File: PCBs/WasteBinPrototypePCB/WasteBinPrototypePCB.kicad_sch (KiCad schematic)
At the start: 0 parts

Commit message: added peltier design to schematic
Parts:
- added D?: D, symbol Device:D
- added D?: DIODE-1N4148, Diode_SMD:D_1206_3216Metric_Pad1.42x1.75mm_HandSolder, symbol SparkFun-DiscreteSemi:DIODE-1N4148
- added D?: LED, symbol Device:LED
- added PE?: PeltierElement, SamacSys_Parts:1808190, symbol Device:PeltierElement
- added Q?: IRL540NSTRLPBF, IRF2804STRLPBF, symbol SamacSys_Parts:IRL540NSTRLPBF
- added R? (x3): 4.7K, symbol Device:R
- added R?: 100, symbol Device:R
- added R?: 1K, symbol Device:R
- added U?: PC817, Package_DIP:DIP-4_W7.62mm, symbol Isolator:PC817
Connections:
- new net: Q?.1, R?.1, R?.1
- new net: D?.2 (A), PE?.2, Q?.3, R?.2
- new net: D?.1 (K), R?.2, U?.3
- new net: R?.1, U?.1
- new net: R?.2, U?.4
- new net: D?.1 (K), R?.1
- new net 12V+: D?.1 (C), D?.2 (A), PE?.1, R?.1
- new net GND: D?.2 (A), Q?.2, R?.2, U?.2
- new net PWM: R?.2
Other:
- note added: "Peltier Element"

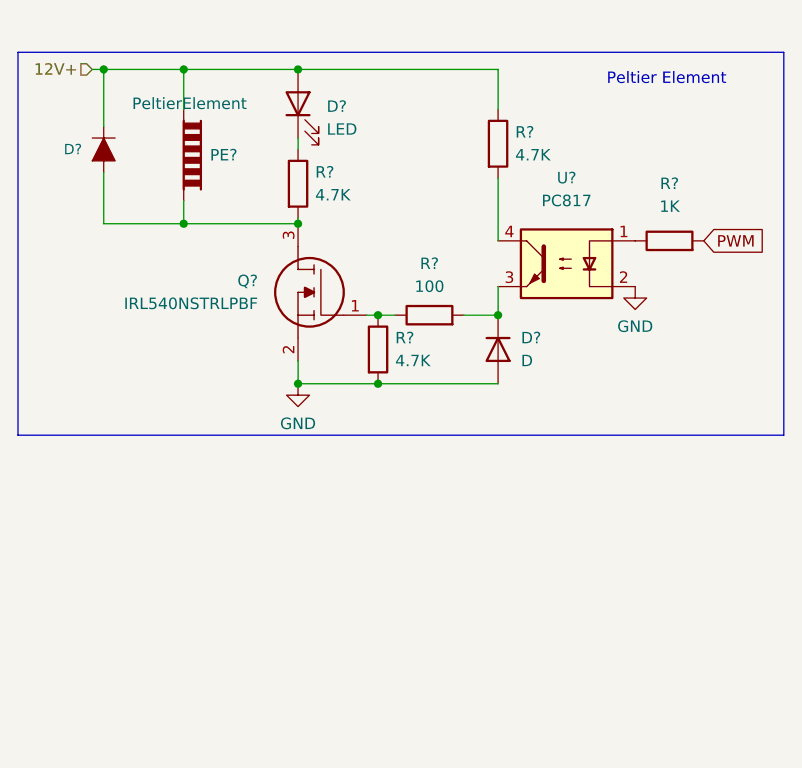
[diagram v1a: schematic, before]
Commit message: added piezo speaker to schematic
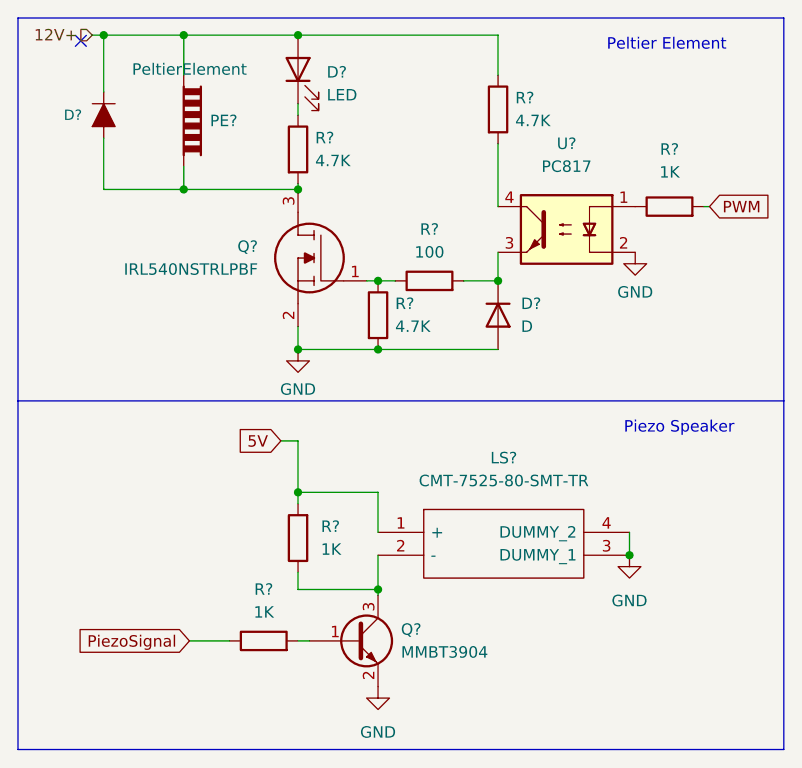
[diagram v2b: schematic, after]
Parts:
- added LS?: CMT-7525-80-SMT-TR, CMT752580SMTTR, symbol SamacSys_Parts:CMT-7525-80-SMT-TR
- added Q?: MMBT3904, Package_TO_SOT_SMD:SOT-23, symbol Transistor_BJT:MMBT3904
- added R? (x2): 1K, symbol Device:R
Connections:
- net GND: now also LS?.3 (DUMMY_1), LS?.4 (DUMMY_2), Q?.2 (E)
- new net: Q?.1 (B), R?.2
- new net: LS?.2 (-), Q?.3 (C), R?.1
- new net 5V: LS?.1 (+), R?.2
- new net PiezoSignal: R?.1
- no-connect marks 0 -> 1
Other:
- note added: "Piezo Speaker"
- moved on the sheet: D?, PE?, Q?, R?, U?

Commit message: added Hall effect sensor to schematic
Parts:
- added R?: 10K, symbol Device:R
- added U?: A1301EUA-T, symbol Sensor_Magnetic:A1301EUA-T
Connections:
- net 5V: now also R?.2, U?.1 (VCC)
- net GND: now also U?.2 (GND)
- new net HES: R?.1, U?.3 (VOUT)
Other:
- note added: "Hall Effect Sensor"
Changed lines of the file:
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@@
   (junction (at 43.815 14.605) (diameter 0) (color 0 0 0 0)
+  )
+  (junction (at 52.07 115.57) (diameter 0) (color 0 0 0 0)
   )
   (junction (at 43.815 49.53) (diameter 0) (color 0 0 0 0)
@@
     (stroke (width 0) (type default) (color 0 0 0 0))
   )
+  (wire (pts (xy 52.07 118.745) (xy 53.975 118.745))
+    (stroke (width 0) (type default) (color 0 0 0 0))
+  )
   (wire (pts (xy 43.815 31.115) (xy 43.815 31.75))
     (stroke (width 0) (type default) (color 0 0 0 0))
   )
+  (wire (pts (xy 52.07 114.935) (xy 52.07 115.57))
+    (stroke (width 0) (type default) (color 0 0 0 0))
+  )
   (wire (pts (xy 43.815 23.495) (xy 43.815 22.225))
     (stroke (width 0) (type default) (color 0 0 0 0))
@@
     (stroke (width 0) (type default) (color 0 0 0 0))
   )
+  (polyline (pts (xy 97.79 93.98) (xy 97.79 123.825))
+    (stroke (width 0) (type default) (color 0 0 0 0))
+  )
+  (wire (pts (xy 52.07 115.57) (xy 52.07 118.745))
+    (stroke (width 0) (type default) (color 0 0 0 0))
+  )
   (wire (pts (xy 31.75 81.915) (xy 36.195 81.915))
     (stroke (width 0) (type default) (color 0 0 0 0))
@@
     (stroke (width 0) (type default) (color 0 0 0 0))
   )
+  (wire (pts (xy 52.07 115.57) (xy 62.23 115.57))
+    (stroke (width 0) (type default) (color 0 0 0 0))
+  )
   (wire (pts (xy 43.815 65.405) (xy 43.815 59.69))
     (stroke (width 0) (type default) (color 0 0 0 0))
@@
     (stroke (width 0) (type default) (color 0 0 0 0))
   )
+  (polyline (pts (xy 97.79 123.825) (xy 12.7 123.825))
+    (stroke (width 0) (type default) (color 0 0 0 0))
+  )
   (wire (pts (xy 52.705 76.835) (xy 52.705 76.2))
     (stroke (width 0) (type default) (color 0 0 0 0))
@@
     (stroke (width 0) (type default) (color 0 0 0 0))
   )
+  (polyline (pts (xy 12.7 123.825) (xy 12.7 93.98))
+    (stroke (width 0) (type default) (color 0 0 0 0))
+  )
   (wire (pts (xy 52.705 65.405) (xy 43.815 65.405))
     (stroke (width 0) (type default) (color 0 0 0 0))
@@
     (stroke (width 0) (type default) (color 0 0 0 0))
   )
+  (wire (pts (xy 62.23 107.95) (xy 62.23 104.775))
+    (stroke (width 0) (type default) (color 0 0 0 0))
+  )
   (polyline (pts (xy 97.79 55.245) (xy 97.79 12.7))
     (stroke (width 0) (type default) (color 0 0 0 0))
@@
   (wire (pts (xy 43.815 14.605) (xy 66.04 14.605))
     (stroke (width 0) (type default) (color 0 0 0 0))
+  )
+  (text "Hall Effect Sensor" (at 77.47 97.155 0)
+    (effects (font (size 1.27 1.27)) (justify left bottom))
   )
   (text "Peltier Element" (at 78.105 16.51 0)
@@
     )
   )
+  (global_label "5V" (shape input) (at 62.23 104.775 0) (fields_autoplaced)
+    (effects (font (size 1.27 1.27)) (justify left))
+    (property "Intersheet References" "${INTERSHEET_REFS}" (id 0) (at 66.9412 104.6956 0)
+      (effects (font (size 1.27 1.27)) (justify left) hide)
+    )
+  )
+  (global_label "HES" (shape input) (at 53.975 118.745 0) (fields_autoplaced)
+    (effects (font (size 1.27 1.27)) (justify left))
+    (property "Intersheet References" "${INTERSHEET_REFS}" (id 0) (at 60.0771 118.6656 0)
+      (effects (font (size 1.27 1.27)) (justify left) hide)
+    )
+  )
   (hierarchical_label "12V+" (shape input) (at 20.955 14.605 180)
     (effects (font (size 1.27 1.27)) (justify right))
@@
     )
     (property "Datasheet" "~" (id 3) (at 52.705 45.72 0)
+      (effects (font (size 1.27 1.27)) hide)
+    )
+    (pin "1")
+    (pin "2")
+  )
+  (symbol (lib_id "Device:R") (at 62.23 111.76 180) (unit 1)
+    (in_bom yes) (on_board yes) (fields_autoplaced)
+    (property "Reference" "R?" (id 0) (at 64.135 110.4899 0)
+      (effects (font (size 1.27 1.27)) (justify right))
+    )
+    (property "Value" "10K" (id 1) (at 64.135 113.0299 0)
+      (effects (font (size 1.27 1.27)) (justify right))
+    )
+    (property "Footprint" "" (id 2) (at 64.008 111.76 90)
+      (effects (font (size 1.27 1.27)) hide)
+    )
+    (property "Datasheet" "~" (id 3) (at 62.23 111.76 0)
       (effects (font (size 1.27 1.27)) hide)
     )
@@
     (pin "1")
     (pin "2")
+  )
+  (symbol (lib_id "power:GND") (at 41.91 104.775 0) (unit 1)
+    (in_bom yes) (on_board yes) (fields_autoplaced)
+    (property "Reference" "#PWR?" (id 0) (at 41.91 111.125 0)
+      (effects (font (size 1.27 1.27)) hide)
+    )
+    (property "Value" "GND" (id 1) (at 41.91 109.855 0))
+    (property "Footprint" "" (id 2) (at 41.91 104.775 0)
+      (effects (font (size 1.27 1.27)) hide)
+    )
+    (property "Datasheet" "" (id 3) (at 41.91 104.775 0)
+      (effects (font (size 1.27 1.27)) hide)
+    )
+    (pin "1")
   )
   (symbol (lib_id "power:GND") (at 80.645 72.39 0) (unit 1)
@@
     (pin "1")
   )
+  (symbol (lib_id "Sensor_Magnetic:A1301EUA-T") (at 52.07 107.315 270) (unit 1)
+    (in_bom yes) (on_board yes) (fields_autoplaced)
+    (property "Reference" "U?" (id 0) (at 52.07 96.52 90))
+    (property "Value" "A1301EUA-T" (id 1) (at 52.07 99.06 90))
+    (property "Footprint" "" (id 2) (at 43.18 107.315 0)
+      (effects (font (size 1.27 1.27) italic) (justify left) hide)
+    )
+    (property "Datasheet" "http://www.allegromicro.com/~/media/Files/Datasheets/A1301-2-Datasheet.ashx" (id 3) (at 52.07 104.775 0)
+      (effects (font (size 1.27 1.27)) hide)
+    )
+    (pin "1")
+    (pin "2")
+    (pin "3")
+  )
   (symbol (lib_id "Device:LED") (at 43.815 18.415 90) (unit 1)
     (in_bom yes) (on_board yes) (fields_autoplaced)
@@
       (reference "#PWR?") (unit 1) (value "GND") (footprint "")
     )
+    (path "/5a17defd-9142-4224-865d-f4648153ba82"
+      (reference "#PWR?") (unit 1) (value "GND") (footprint "")
+    )
     (path "/666e1366-8b99-45ca-af58-37cd07d0f351"
       (reference "#PWR?") (unit 1) (value "GND") (footprint "")
@@
       (reference "R?") (unit 1) (value "4.7K") (footprint "")
     )
+    (path "/23a0a120-4468-43ee-9d86-86770507e5ab"
+      (reference "R?") (unit 1) (value "10K") (footprint "")
+    )
     (path "/4583b515-ed49-4672-843a-9aa019653137"
       (reference "R?") (unit 1) (value "100") (footprint "")
@@
       (reference "U?") (unit 1) (value "PC817") (footprint "Package_DIP:DIP-4_W7.62mm")
     )
-  )
+    (path "/d6911078-c811-4b16-81c1-2d59c3e06949"
+      (reference "U?") (unit 1) (value "A1301EUA-T") (footprint "")
+    )
+  )

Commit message: improved on documentation and design
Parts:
- added C? (x2): 2.2uF 25V, symbol Device:C
- added IC?: MCP1793T-3302H_OT, SOT95P280X145-5N, symbol SamacSys_Parts:MCP1793T-3302H_OT
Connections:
- net 12V+: now also C?.2, IC?.1 (VIN), IC?.3 (~{SHDN})
- net GND: now also C?.1, C?.2, IC?.2 (GND)
- net 5V renamed 3.3V
- net 3.3V: now also C?.1, IC?.5 (VOUT)
- no-connect marks 1 -> 0
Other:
- note added: "Vragen voor insyte: -ESP32 devkit direct op pcb (d.m.v. headers)? -> scheelt ontwerptijd en geeft flexibiliteit -Handsolderen of pcb asemblage door bedrijf? -temperatuur sensor plaatsing en type (SHT40 of goedkoper alternatief?) -klep sensor (HES), plaatsing en beeld hierover. -2 printplaten 1 als devkit en 1 voor eindresultaat."

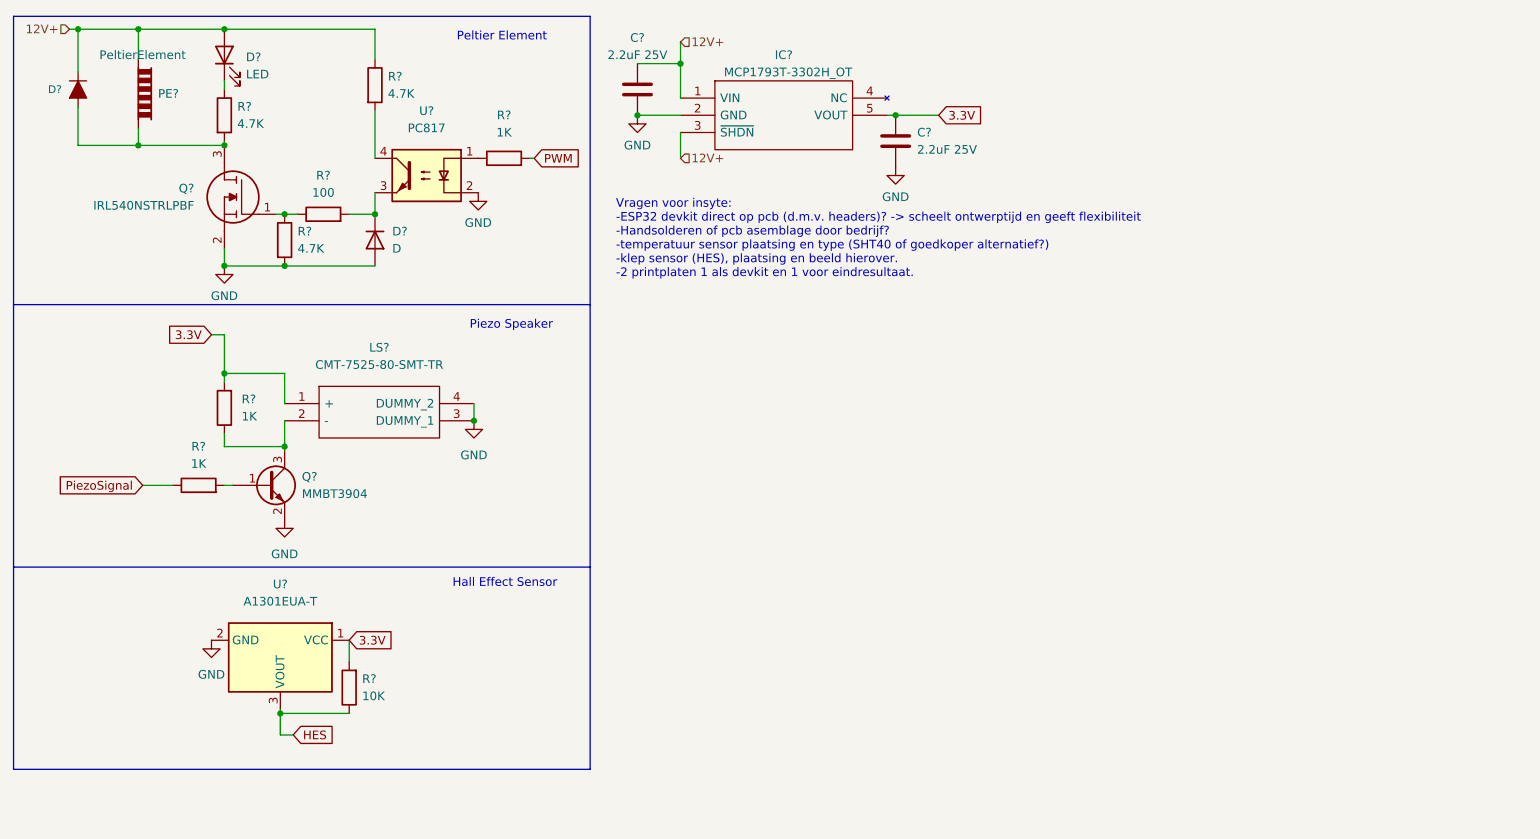
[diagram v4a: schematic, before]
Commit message: added microcontroller, breakout headers, 5V regulator and i2c vreakout to schematic
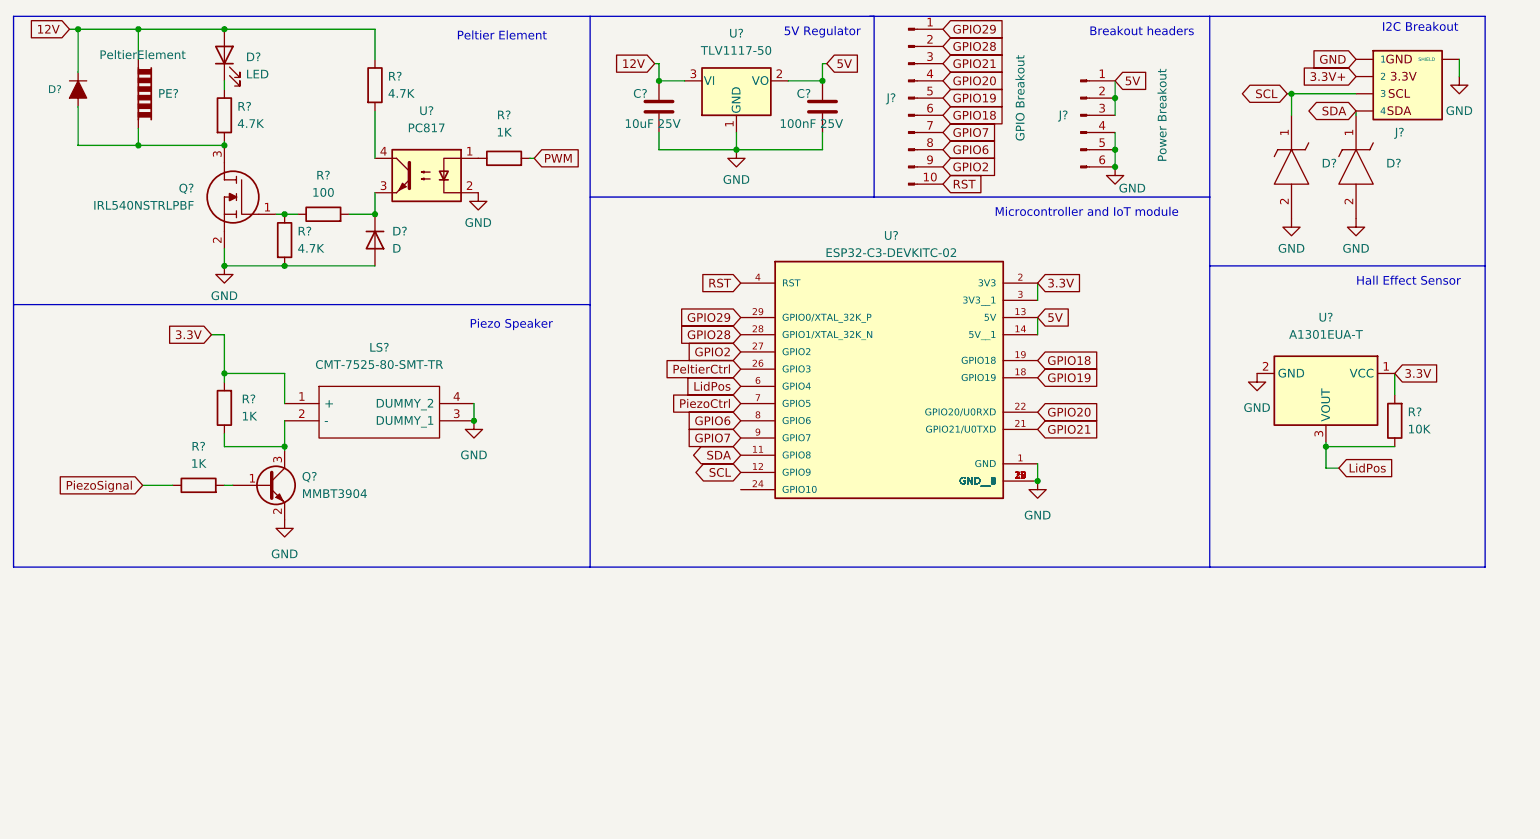
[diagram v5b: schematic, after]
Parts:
- removed C? (x2): 2.2uF 25V, symbol Device:C
- removed IC?: MCP1793T-3302H_OT, SOT95P280X145-5N, symbol SamacSys_Parts:MCP1793T-3302H_OT
- added C?: 100nF 25V, Capacitor_SMD:C_0805_2012Metric_Pad1.18x1.45mm_HandSolder, symbol Device:C
- added C?: 10uF 25V, Capacitor_SMD:C_0805_2012Metric_Pad1.18x1.45mm_HandSolder, symbol Device:C
- added D? (x2): ESD7351HT1G, SamacSys_Parts:SOD2512X110N, symbol SamacSys_Parts:ESD7351HT1G
- added J?: Conn_01x06_Male, symbol Connector:Conn_01x06_Male
- added J?: SM04B-SRSS-TB(LF)(SN), SnapEDA Library:JST_SM04B-SRSS-TB(LF)(SN), symbol SM04B-SRSS-TB_LF__SN_:SM04B-SRSS-TB(LF)(SN)
- added J?: Conn_01x10_Male, symbol Connector:Conn_01x10_Male
- added U?: TLV1117-50, symbol Regulator_Linear:TLV1117-50
- added U?: ESP32-C3-DEVKITC-02, SnapEDA Library:XCVR_ESP32-C3-DEVKITC-02, symbol ESP32-C3-DEVKITC-02:ESP32-C3-DEVKITC-02
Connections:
- net 3.3V: now also U?.2 (3V3), U?.3 (3V3__1)
- net GND: now also C?.1, C?.2, D?.2, D?.2, J?.1, J?.4 (Pin_4), J?.5 (Pin_5), J?.6 (Pin_6), J?.S1 (SHIELD), J?.S2 (SHIELD), U?.1 (GND), U?.1 (GND), U?.10 (GND__2), U?.15 (GND__3), U?.16 (GND__4), U?.17 (GND__5), U?.20 (GND__6), U?.23 (GND__7), U?.25 (GND__8), U?.30 (GND__9), U?.5 (GND__1)
- net 12V+ renamed 12V
- net 12V: now also C?.1, U?.3 (VI)
- net HES renamed LidPos
- net LidPos: now also U?.6 (GPIO4)
- new net 3.3V+: J?.2
- new net 5V: C?.2, J?.1 (Pin_1), J?.2 (Pin_2), J?.3 (Pin_3), U?.13 (5V), U?.14 (5V__1), U?.2 (VO)
- new net GPIO18: J?.6 (Pin_6), U?.19 (GPIO18)
- new net GPIO19: J?.5 (Pin_5), U?.18 (GPIO19)
- new net GPIO2: J?.9 (Pin_9), U?.27 (GPIO2)
- new net GPIO20: J?.4 (Pin_4), U?.22 (GPIO20/U0RXD)
- new net GPIO21: J?.3 (Pin_3), U?.21 (GPIO21/U0TXD)
- new net GPIO28: J?.2 (Pin_2), U?.28 (GPIO1/XTAL_32K_N)
- new net GPIO29: J?.1 (Pin_1), U?.29 (GPIO0/XTAL_32K_P)
- new net GPIO6: J?.8 (Pin_8), U?.8 (GPIO6)
- new net GPIO7: J?.7 (Pin_7), U?.9 (GPIO7)
- new net PeltierCtrl: U?.26 (GPIO3)
- new net PiezoCtrl: U?.7 (GPIO5)
- new net RST: J?.10 (Pin_10), U?.4 (RST)
- new net SCL: D?.1, J?.3, U?.12 (GPIO9)
- new net SDA: D?.1, J?.4, U?.11 (GPIO8)
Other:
- note added: "5V Regulator"
- note added: "Breakout headers"
- note added: "I2C Breakout"
- note added: "Microcontroller and IoT module"
- note removed: "Vragen voor insyte: -ESP32 devkit direct op pcb (d.m.v. headers)? -> scheelt ontwerptijd en geeft flexibiliteit -Handsolderen of pcb asemblage door bedrijf? -temperatuur sensor plaatsing en type (SHT40 of goedkoper alternatief?) -klep sensor (HES), plaatsing en beeld hierover. -2 printplaten 1 als devkit en 1 voor eindresultaat."
- moved on the sheet: R?, U?

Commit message: added Power input
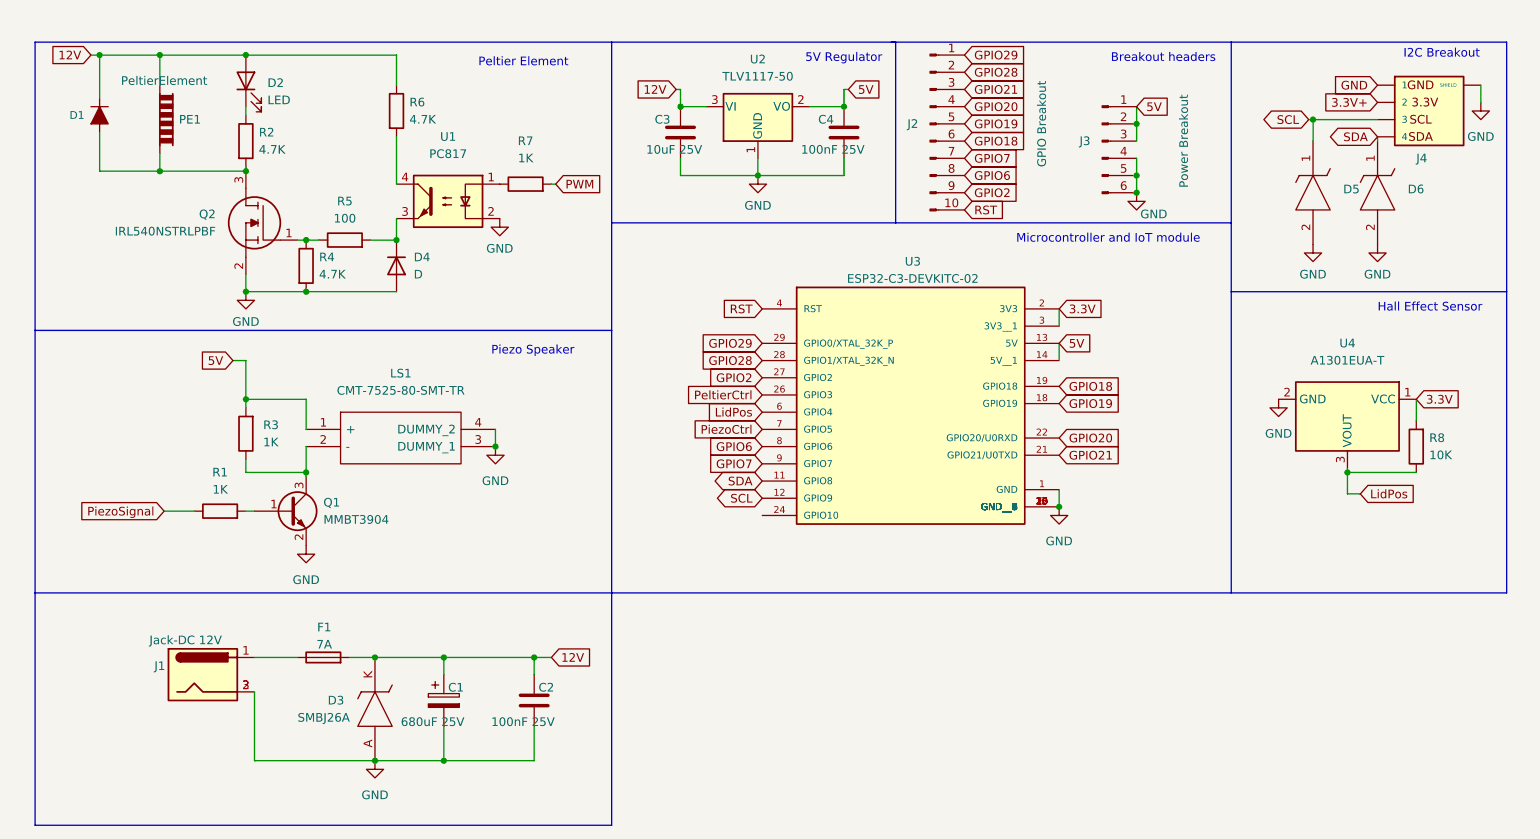
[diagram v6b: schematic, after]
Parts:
- added C1: 680uF 25V, Capacitor_SMD:CP_Elec_8x10, symbol Device:C_Polarized
- added C2: 100nF 25V, Capacitor_SMD:C_0805_2012Metric_Pad1.18x1.45mm_HandSolder, symbol Device:C
- added D3: SMBJ26A, SamacSys_Parts:DIOM5436X261N, symbol SamacSys_Parts:SMBJ26A
- added F1: 7A, Fuse:Fuse_2010_5025Metric_Pad1.52x2.65mm_HandSolder, symbol Device:Fuse
- added J1: Jack-DC 12V, Connector_BarrelJack:BarrelJack_Wuerth_6941xx301002, symbol Connector:Jack-DC
- gave numbers to parts that had none: 26
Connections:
- net 12V: now also C1.1, C2.1, D3.K, F1.2
- net 3.3V: no longer LS1.1 (+), R3.2
- net 5V: now also LS1.1 (+), R3.2
- net GND: now also C1.2, C2.2, D3.A, J1.2, J1.3
- new net: F1.1, J1.1
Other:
- moved on the sheet: C3, C4, D1, D2, D4, D5, D6, J2, J3, J4, LS1, PE1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
